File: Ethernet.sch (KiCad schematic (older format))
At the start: 46 parts, among them J3 100BaseT1, J6 Conn_01x08_Female, U1 LPC54616J512, U2 DP83TC811R-Q1, U3 74LVC1G04, Y2 25 MHz

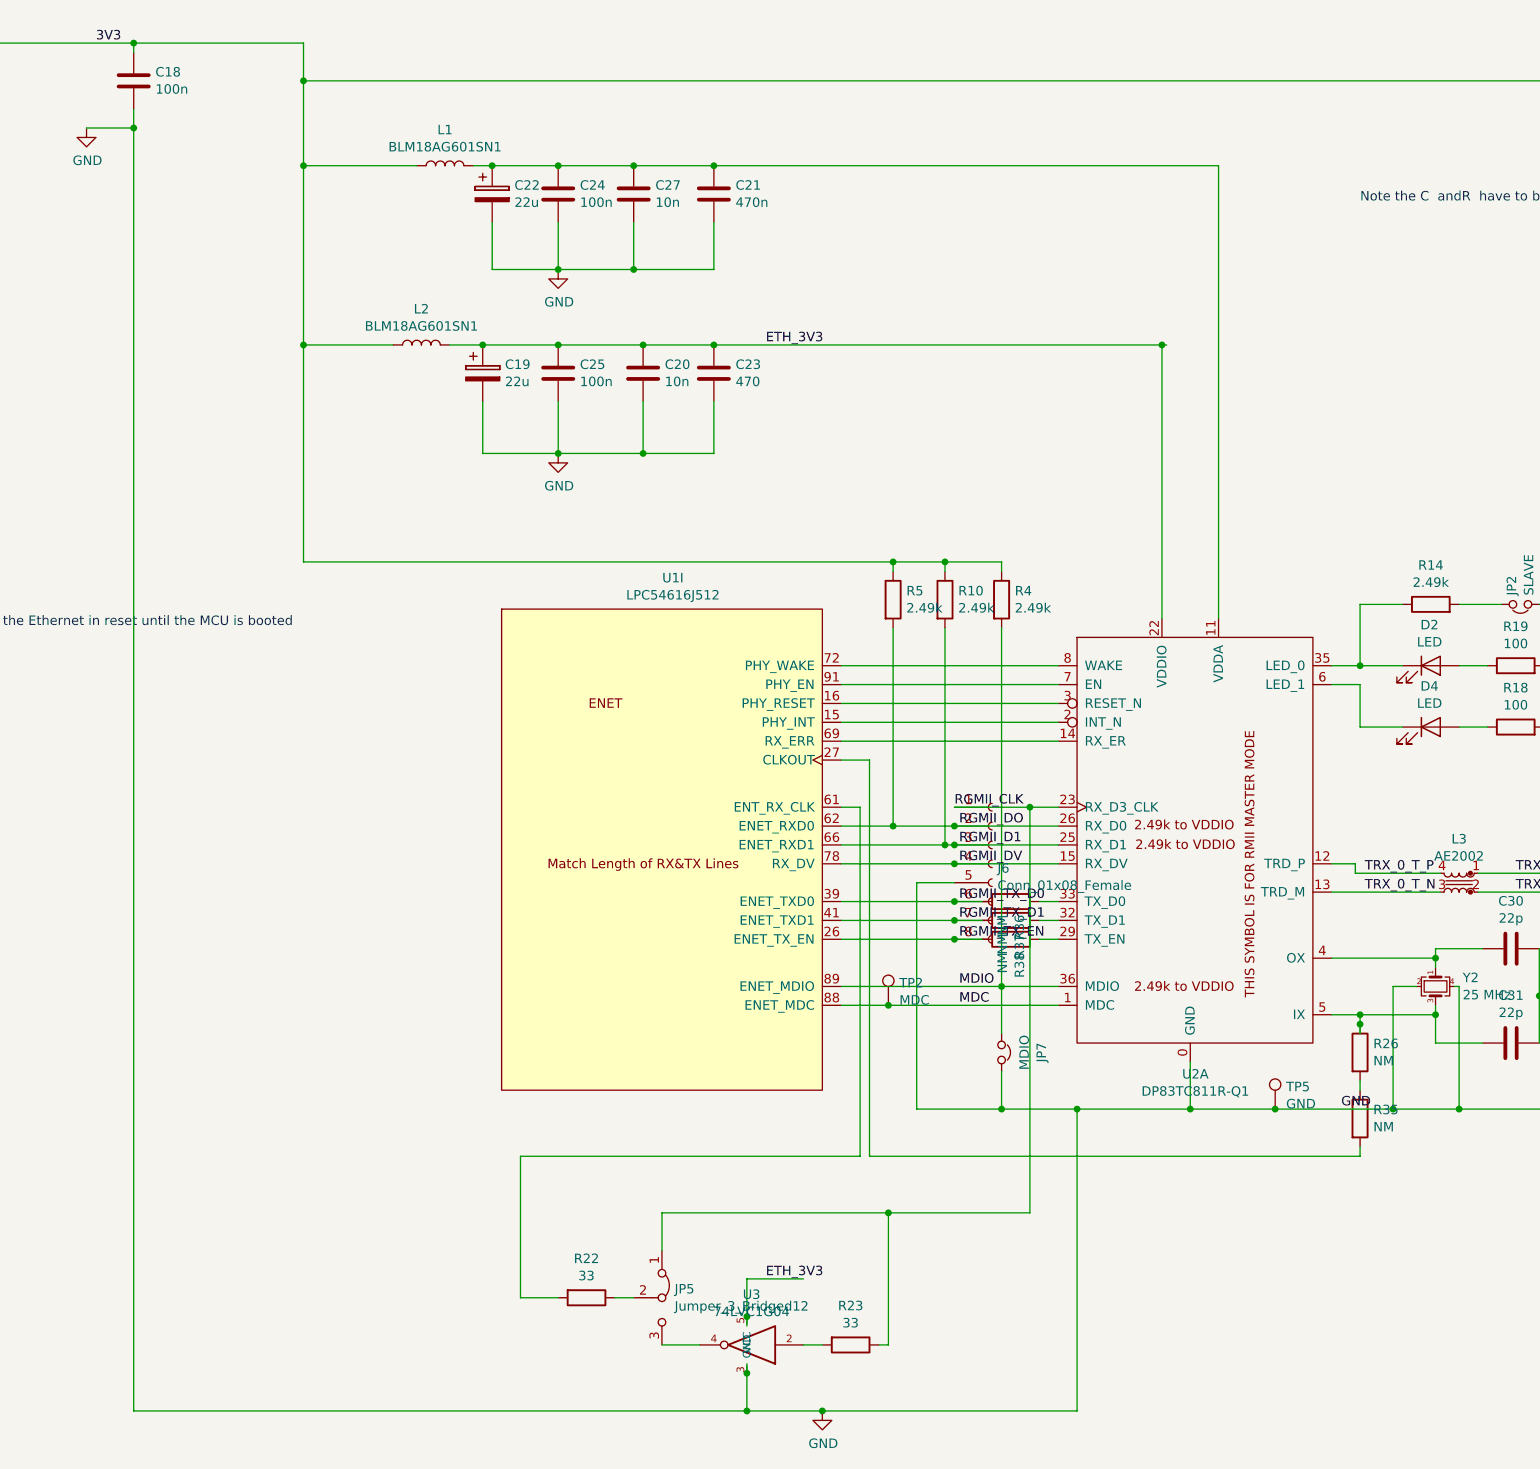
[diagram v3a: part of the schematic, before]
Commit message: Switch to 4 Layer PCB as the RMII loopback doesn't work
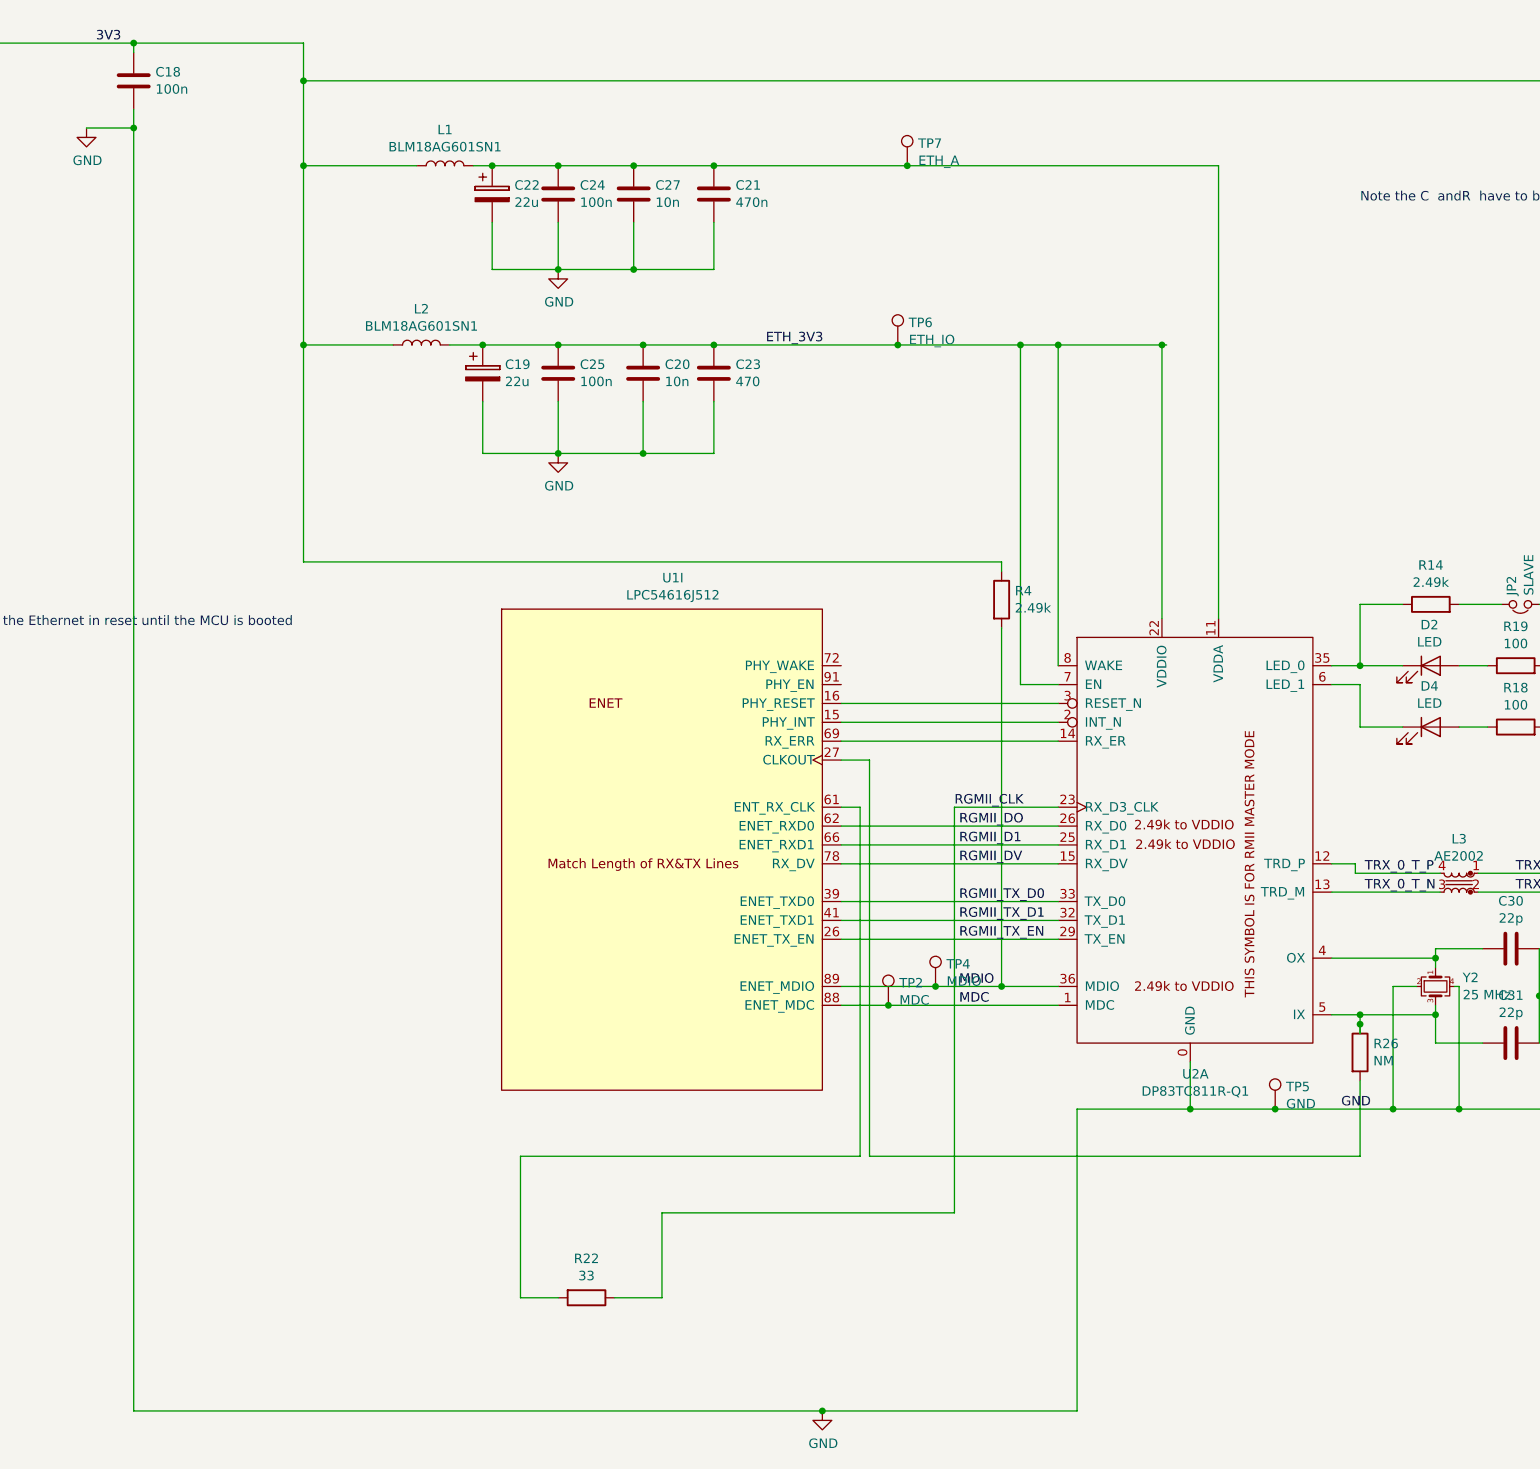
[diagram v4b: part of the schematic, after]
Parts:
- removed J6: Conn_01x08_Female, Connector_PinHeader_1.27mm:PinHeader_1x08_P1.27mm_Vertical_RMII, symbol Connector:Conn_01x08_Female
- removed JP5: Jumper_3_Bridged12, Jumper:SolderJumper-3_P1.3mm_Open_RoundedPad1.0x1.5mm, symbol Jumper:Jumper_3_Bridged12
- removed JP7: MDIO, Connector_PinHeader_2.54mm:PinHeader_1x02_P2.54mm_Vertical, symbol canbox-rescue:Jumper_NC_Small-Device
- removed R10, R5: 2.49k, Resistor_SMD:R_0805_2012Metric_Pad1.15x1.40mm_HandSolder, symbol canbox-rescue:R-Device
- removed R23: 33, Resistor_SMD:R_0805_2012Metric_Pad1.15x1.40mm_HandSolder, symbol Device:R
- removed R35, R36, R37, R38: NM, Resistor_SMD:R_0805_2012Metric_Pad1.15x1.40mm_HandSolder, symbol canbox-rescue:R-Device
- removed U3: 74LVC1G04, Package_TO_SOT_SMD:SOT-353_SC-70-5_Handsoldering, symbol 74xGxx:74LVC1G04
- added TP4: MDIO, TestPoint:TestPoint_THTPad_1.5x1.5mm_Drill0.7mm, symbol Connector:TestPoint
- added TP6: ETH_IO, TestPoint:TestPoint_THTPad_1.5x1.5mm_Drill0.7mm, symbol Connector:TestPoint
- added TP7: ETH_A, TestPoint:TestPoint_THTPad_1.5x1.5mm_Drill0.7mm, symbol Connector:TestPoint
- C32, C33: footprint Capacitor_SMD:C_0805_2012Metric_Pad1.15x1.40mm_HandSolder -> Capacitor_SMD:C_0603_1608Metric_Pad1.05x0.95mm_HandSolder
- JP3: footprint Jumper:SolderJumper-2_P1.3mm_Open_Pad1.0x1.5mm -> Connector_PinHeader_2.54mm:PinHeader_1x02_P2.54mm_Vertical
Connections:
- wire segments 173 -> 143

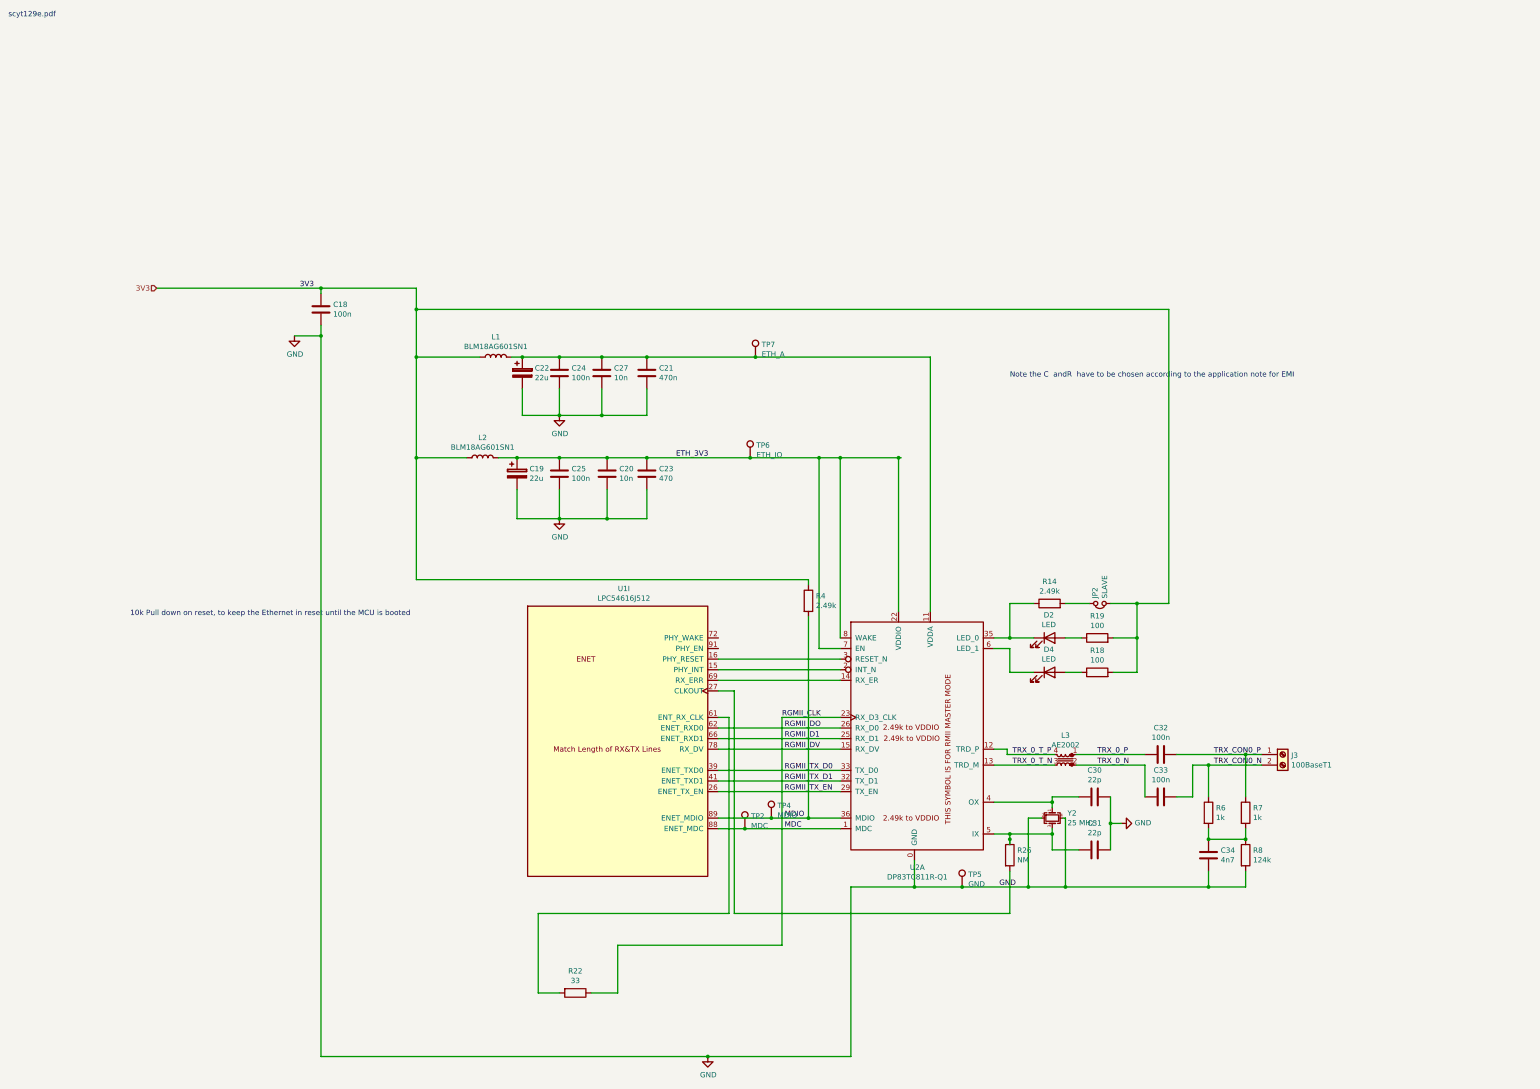
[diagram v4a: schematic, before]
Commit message: V5 now impedance controlled
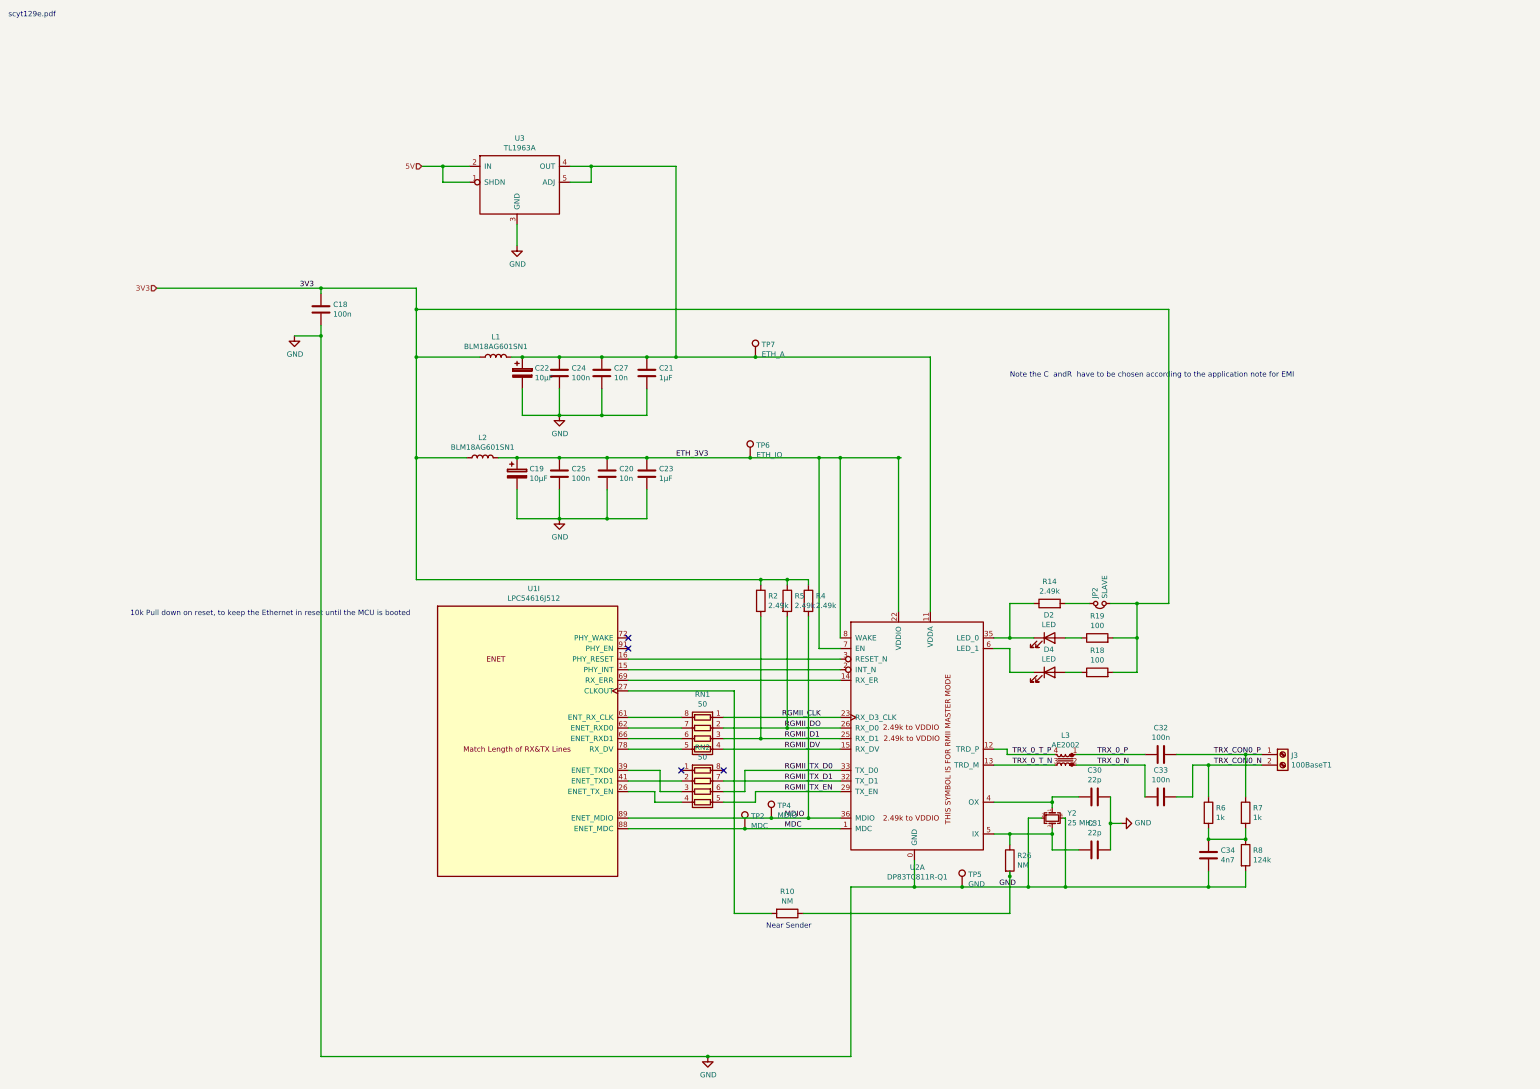
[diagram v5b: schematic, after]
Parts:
- removed R22: 33, Resistor_SMD:R_0805_2012Metric_Pad1.15x1.40mm_HandSolder, symbol Device:R
- added R10: NM, Resistor_SMD:R_0805_2012Metric_Pad1.15x1.40mm_HandSolder, symbol canbox-rescue:R-Device
- added R2, R5: 2.49k, Resistor_SMD:R_0402_1005Metric, symbol canbox-rescue:R-Device
- added RN1, RN2: 50, Resistor_SMD:R_Array_Concave_4x0603, symbol Device:R_Pack04
- added U3: TL1963A, Package_TO_SOT_SMD:TO-263-5_TabPin3, symbol cypress:TL1963A
- C19, C22: value 22u -> 10µF
- C21: value 470n -> 1µF
- C23: value 470 -> 1µF
- L3: footprint Inductor_SMD:L_CMC_1812 -> cypress:L_CMC_1812
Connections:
- net 3V3: now also R2.1, R5.1
- net GND: now also U3.3 (GND)
- net RGMII_CLK: now also RN1.1 (R1.1)
- net RGMII_D1: now also R2.2, RN1.3 (R3.1); no longer U1.66 (ENET_RXD1)
- net RGMII_DO: now also R5.2, RN1.2 (R2.1); no longer U1.62 (ENET_RXD0)
- net RGMII_DV: now also RN1.4 (R4.1); no longer U1.78 (RX_DV)
- net RGMII_TX_D0: now also RN2.6 (R3.2); no longer U1.39 (ENET_TXD0)
- net RGMII_TX_D1: now also RN2.7 (R2.2); no longer U1.41 (ENET_TXD1)
- net RGMII_TX_EN: now also RN2.5 (R4.2); no longer U1.26 (ENET_TX_EN)
- net at U1.27 (CLKOUT): now also R10.2; no longer R26.2
- net at U1.61 (ENT_RX_CLK): now also RN1.8 (R1.2)
- net at C21.1, C22.1, C24.1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: now also U3.4 (OUT), U3.5 (ADJ)
- new net: RN2.4 (R4.1), U1.26 (ENET_TX_EN)
- new net: RN2.3 (R3.1), U1.39 (ENET_TXD0)
- new net: RN2.2 (R2.1), U1.41 (ENET_TXD1)
- new net: RN1.7 (R2.2), U1.62 (ENET_RXD0)
- new net: RN1.6 (R3.2), U1.66 (ENET_RXD1)
- new net: RN1.5 (R4.2), U1.78 (RX_DV)
- new net: R10.1, R26.2
- new net 5V: U3.1 (SHDN), U3.2 (IN)
- no-connect marks 0 -> 4
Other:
- note added: "Near Sender"
- moved on the sheet: R26, U1I
